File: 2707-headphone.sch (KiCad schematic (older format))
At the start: 24 parts, among them SW1 SPST, SW2 SPST, SW3 SPST, SW4 SPST, SW5 SPST, SW6 SPST, SW7 SPST, U1 PCM2707, X1 CRYSTAL, X2 USB-B-H

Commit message: made hierarchy
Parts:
- removed C1: CP1, symbol CP1
- removed C2, C3, C4, C5, C6, C7, C8: C, symbol C
- removed R1, R2, R3, R4, R5: R, symbol R
- removed SW1, SW2, SW3, SW4, SW5, SW6, SW7: SPST, symbol SPST
- removed U1: PCM2707, SMD_Packages:TQFP32, symbol PCM2707
- removed X1: CRYSTAL, symbol CRYSTAL
- removed X2: USB-B-H, con-usb-USB-B-H, symbol USB-B-H
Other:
- moved on the sheet: LOGO1

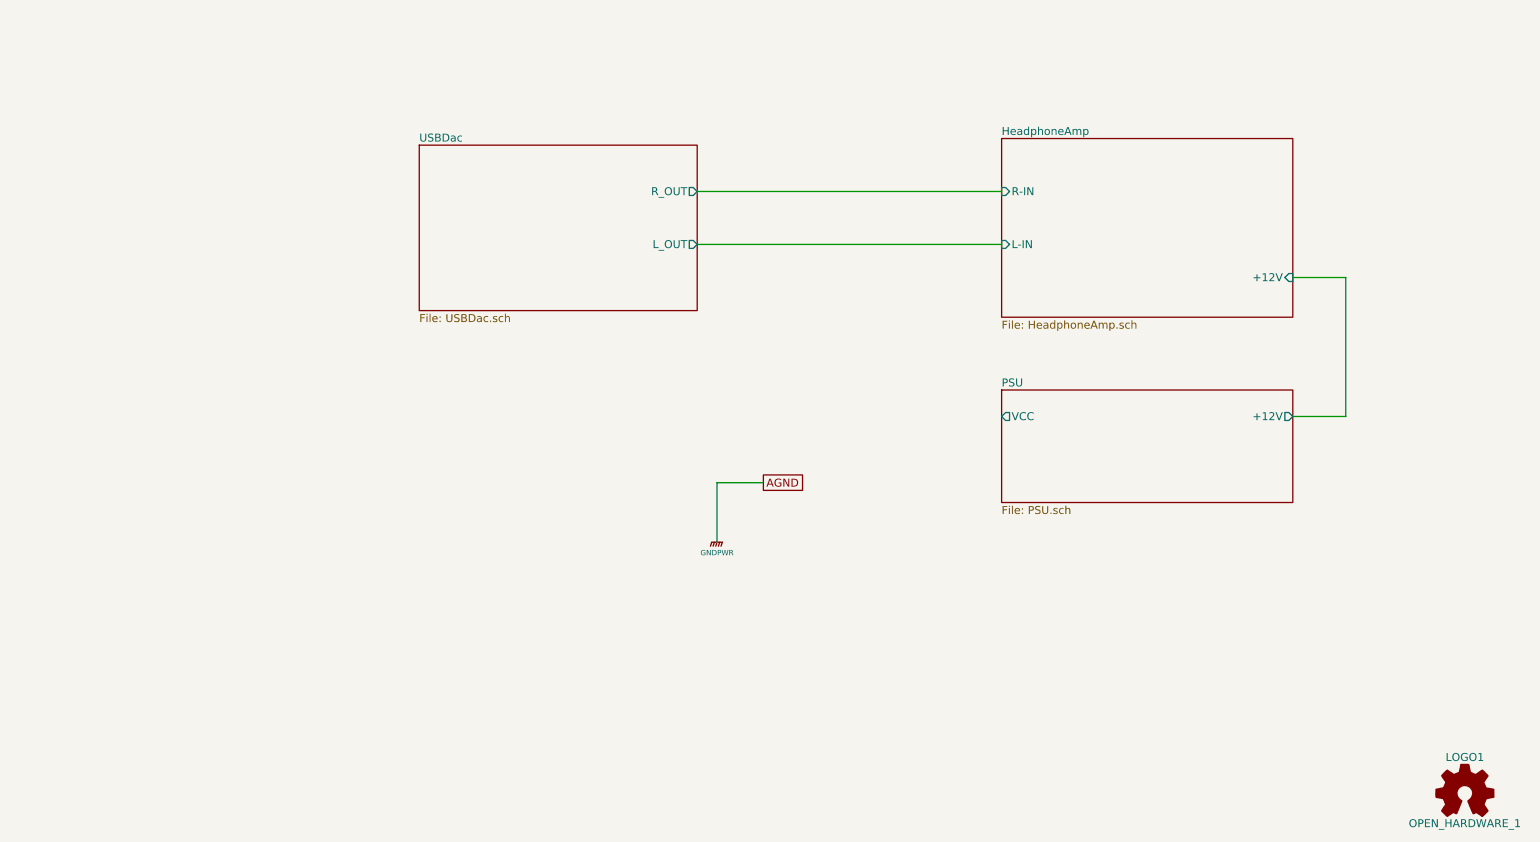
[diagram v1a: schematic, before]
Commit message: redrawn plus crossfeed, still needs PSU
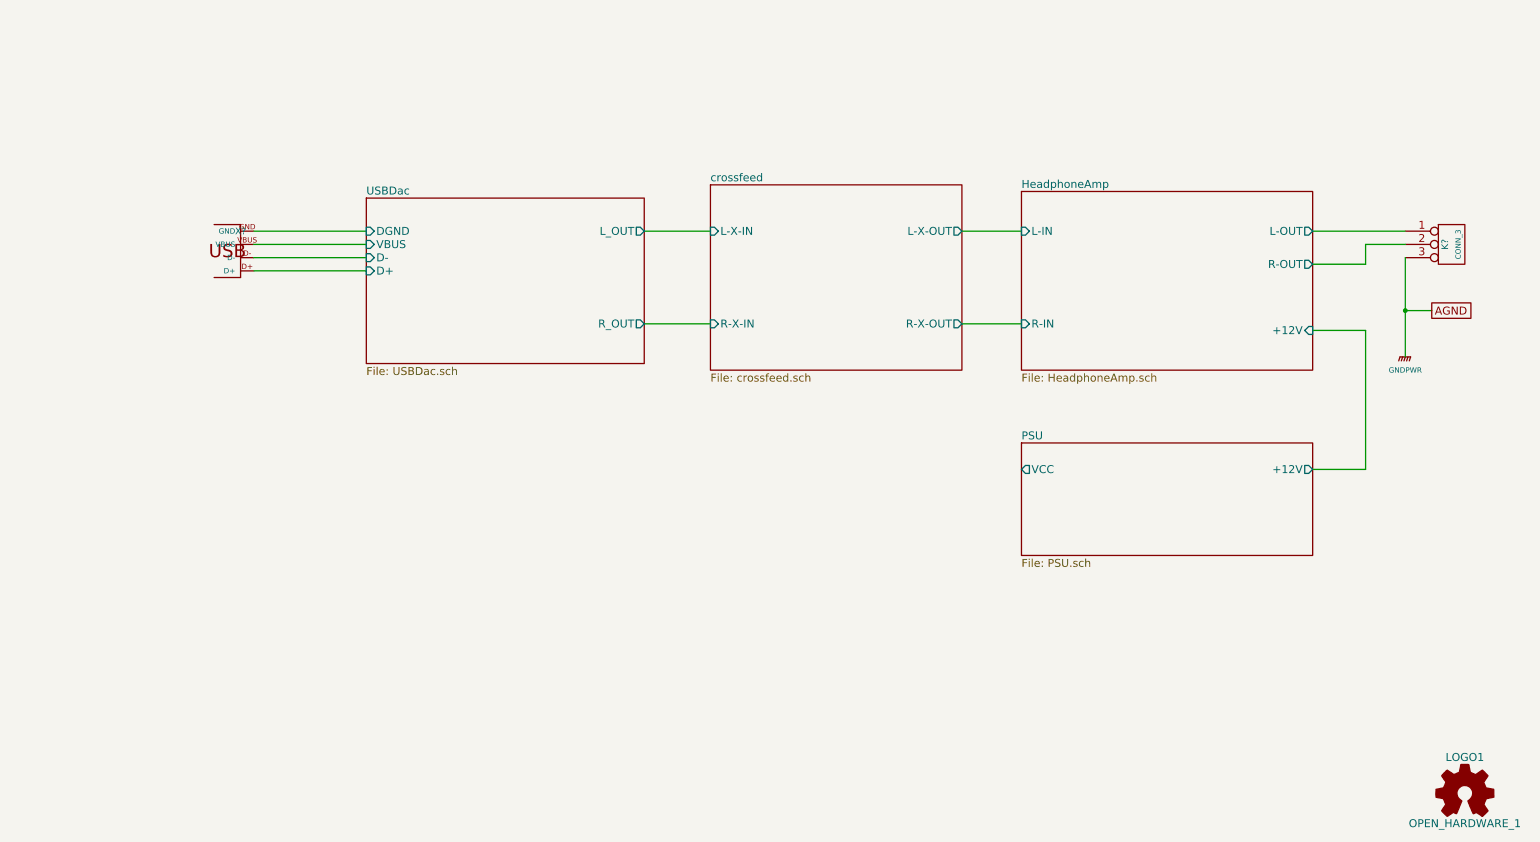
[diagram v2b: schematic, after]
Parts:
- added K?: CONN_3, symbol CONN_3
- added X?: USB-B-H, con-usb-USB-B-H, symbol USB-B-H
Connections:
- net GNDPWR: now also K?.3 (P3)
- new net HeadphoneAmp/L-OUT: K?.1 (P1)
- new net HeadphoneAmp/R-OUT: K?.2 (PM)
- new net USBDac/D+: X?.D+
- new net USBDac/D-: X?.D-
- new net USBDac/DGND: X?.GND
- new net USBDac/VBUS: X?.VBUS
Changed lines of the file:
@@
 LIBS:audio
 LIBS:con-usb
+LIBS:v-reg
+LIBS:conn
 LIBS:2707-headphone-cache
 EELAYER 24 0
@@
 $Descr A4 11693 8268
 encoding utf-8
-Sheet 1 4
+Sheet 1 5
 Title "2707 Headphone DAC"
-Date "19 Jul 2014"
+Date "22 Jul 2014"
 Rev "0.1"
 Comp "Xav Paice"
@@
 $EndComp
 $Sheet
-S 6900 1900 2200 1350
+S 7050 2300 2200 1350
 U 53CA4D1D
 F0 "HeadphoneAmp" 60
 F1 "HeadphoneAmp.sch" 60
-F2 "L-IN" I L 6900 2700 60
-F3 "R-IN" I L 6900 2300 60
-F4 "+12V" I R 9100 2950 60
+F2 "L-IN" I L 7050 2600 60
+F3 "R-IN" I L 7050 3300 60
+F4 "+12V" I R 9250 3350 60
+F5 "L-OUT" O R 9250 2600 60
+F6 "R-OUT" O R 9250 2850 60
 $EndSheet
 $Sheet
-S 6900 3800 2200 850
+S 7050 4200 2200 850
 U 53CA4E95
 F0 "PSU" 60
 F1 "PSU.sch" 60
-F2 "VCC" O L 6900 4000 60
-F3 "+12V" O R 9100 4000 60
+F2 "VCC" O L 7050 4400 60
+F3 "+12V" O R 9250 4400 60
 $EndSheet
 $Sheet
-S 2500 1950 2100 1250
+S 2100 2350 2100 1250
 U 53CB00DB
 F0 "USBDac" 60
 F1 "USBDac.sch" 60
-F2 "R_OUT" O R 4600 2300 60
-F3 "L_OUT" O R 4600 2700 60
+F2 "R_OUT" O R 4200 3300 60
+F3 "L_OUT" O R 4200 2600 60
+F4 "DGND" I L 2100 2600 60
+F5 "D+" I L 2100 2900 60
+F6 "D-" I L 2100 2800 60
+F7 "VBUS" I L 2100 2700 60
 $EndSheet
-Text GLabel 5100 4500 2    60   UnSpc ~ 0
+Text GLabel 10150 3200 2    60   UnSpc ~ 0
 AGND
 Wire Wire Line
-	9100 2950 9500 2950
+	9250 3350 9650 3350
 Wire Wire Line
-	9500 2950 9500 4000
+	9650 3350 9650 4400
 Wire Wire Line
-	9500 4000 9100 4000
-Wire Wire Line
-	4600 2300 6900 2300
-Wire Wire Line
-	4600 2700 6900 2700
+	9650 4400 9250 4400
 $Comp
 L GNDPWR #PWR1
 U 1 1 53CB6990
-P 4750 4950
-F 0 "#PWR1" H 4750 5000 40  0001 C CNN
-F 1 "GNDPWR" H 4750 4870 40  0000 C CNN
-F 2 "" H 4750 4950 60  0000 C CNN
-F 3 "" H 4750 4950 60  0000 C CNN
-	1    4750 4950
+P 9950 3550
+F 0 "#PWR1" H 9950 3600 40  0001 C CNN
+F 1 "GNDPWR" H 9950 3450 40  0000 C CNN
+F 2 "" H 9950 3550 60  0000 C CNN
+F 3 "" H 9950 3550 60  0000 C CNN
+	1    9950 3550
+	1    0    0    -1
+$EndComp
+$Comp
+L USB-B-H X?
+U 1 1 53CD54E1
+P 1150 2600
+F 0 "X?" H 1150 2600 50  0000 C CNN
+F 1 "USB-B-H" H 1150 2600 50  0001 C CNN
+F 2 "con-usb-USB-B-H" H 1150 2750 50  0001 C CNN
+F 3 "" H 1150 2600 60  0000 C CNN
+	1    1150 2600
+	-1   0    0    1
+$EndComp
+Wire Wire Line
+	1250 2600 2100 2600
+Wire Wire Line
+	1250 2700 2100 2700
+Wire Wire Line
+	1250 2800 2100 2800
+Wire Wire Line
+	1250 2900 2100 2900
+$Sheet
+S 4700 2250 1900 1400
+U 53CE24D0
+F0 "crossfeed" 60
+F1 "crossfeed.sch" 60
+F2 "L-X-IN" I L 4700 2600 60
+F3 "L-X-OUT" O R 6600 2600 60
+F4 "R-X-IN" I L 4700 3300 60
+F5 "R-X-OUT" O R 6600 3300 60
+$EndSheet
+Wire Wire Line
+	4200 2600 4700 2600
+Wire Wire Line
+	6600 2600 7050 2600
+Wire Wire Line
+	4200 3300 4700 3300
+Wire Wire Line
+	6600 3300 7050 3300
+$Comp
+L CONN_3 K?
+U 1 1 53CF4491
+P 10300 2700
+F 0 "K?" V 10250 2700 50  0000 C CNN
+F 1 "CONN_3" V 10350 2700 40  0000 C CNN
+F 2 "" H 10300 2700 60  0000 C CNN
+F 3 "" H 10300 2700 60  0000 C CNN
+	1    10300 2700
 	1    0    0    -1
 $EndComp
 Wire Wire Line
-	5100 4500 4750 4500
+	9950 2800 9950 3550
 Wire Wire Line
-	4750 4500 4750 4950
+	9950 3200 10150 3200
+Connection ~ 9950 3200
+Wire Wire Line
+	9250 2850 9650 2850
+Wire Wire Line
+	9650 2850 9650 2700
+Wire Wire Line
+	9650 2700 9950 2700
+Wire Wire Line
+	9950 2600 9250 2600
 $EndSCHEMATC
